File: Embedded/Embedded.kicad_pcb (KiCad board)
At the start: 2 copper layers, 77.5 x 106.5 mm, 95 parts, among them J1 GyroBreakout, J2 Conn_01x08, J3 Conn_01x08, J6 Conn_01x08, J7 Conn_01x08, SW1 BackboardSw, U1 ESP32-C6-WROOM-1, U2 BQ25895RTW, U3 FSUSB30MUX, U5 MP8715, U7 SN74AHCT125N, U8 SN74AHCT125N

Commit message: v2.1
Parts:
- added ?: , , F.Cu at (177.5, 95.6)
- added ?: , , F.Cu at (176.5, 96.7)
- added ?: , , F.Cu at (176.5, 98.2)
- moved LS1 41.9 mm to (175.0, 138.0), turned to -90 degrees
- moved ? 4.01 mm to (180.5, 95.5)
- moved ? 4.00 mm to (183.5, 95.5)
- moved ? 4.00 mm to (182.0, 95.5)
- moved ? 4.00 mm to (186.5, 95.5)
- moved ? 4.00 mm to (185.0, 95.5)
- moved ? 3.99 mm to (179.0, 95.5)
- moved ? 1.57 mm to (177.2, 111.2)
- moved ? 1.15 mm to (176.4, 99.6)
- moved ? 1.00 mm to (176.2, 110.1)
- moved ? 0.65 mm to (176.3, 108.6)
- moved ? 0.60 mm to (176.3, 107.1)
- moved ? 0.59 mm to (176.4, 101.1)
- moved ? 0.59 mm to (176.3, 105.6)
- moved ? 0.59 mm to (176.3, 102.6)
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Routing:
- net Net-(U1-MTMS/GPIO4/ADC1_CH4): track 0.00 -> 138.5 mm, vias 0 -> 6
- net Net-(U1-GPIO21): track 0.00 -> 118.6 mm, vias 0 -> 4
- net Net-(U1-MTDI/GPIO5/ADC1_CH5): track 60.0 -> 137.1 mm, vias 4 -> 6
- net GND: track 24.2 -> 9.09 mm, vias 50 -> 54
- net Net-(J6-Pin_6): track 28.9 -> 21.0 mm
- net Net-(J1-Pin_8): track 149.9 -> 152.6 mm
- net Net-(J1-Pin_7): track 144.5 -> 146.9 mm
- net +3.3V: track 329.1 -> 327.8 mm
- added copper zone on B.Cu, net GND
- added copper zone on F.Cu, net GND

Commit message: small changes, big dreams
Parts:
- added D1: 1N5819, Diode_THT:D_DO-41_SOD81_P10.16mm_Horizontal, B.Cu at (180.5, 75.4)
- added D2: 1N5819, Diode_THT:D_DO-41_SOD81_P10.16mm_Horizontal, B.Cu at (144.5, 45.0)
- added M1: Fan, Capacitor_SMD:C_1808_4520Metric_Pad1.72x2.30mm_HandSolder, F.Cu at (173.5, 75.5)
- added Q1: FQP27P06, Package_TO_SOT_THT:TO-220-3_Vertical, B.Cu at (173.9, 80.5)
- moved BT1 15.5 mm to (176.0, 92.5), turned to 0 degrees
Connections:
- J1 pad 3: unconnected-(J1-Pin_3-Pad3) -> Net-(J1-Pin_3)
- U1 pad 24: unconnected-(U1-U0RXD/GPIO17-Pad24) -> Net-(J1-Pin_3)
- U1 pad 25: unconnected-(U1-U0TXD/GPIO16-Pad25) -> Net-(Q1-G)
- U7 pad 11: Net-(J3-Pin_7) -> Net-(J3-Pin_4)
- U7 pad 3: Net-(J3-Pin_4) -> Net-(J3-Pin_7)
- U7 pad 6: Net-(J3-Pin_5) -> Net-(J3-Pin_6)
- U7 pad 8: Net-(J3-Pin_6) -> Net-(J3-Pin_5)
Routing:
- net Net-(Q1-G): track 0.00 -> 70.0 mm
- net Net-(J1-Pin_3): track 0.00 -> 30.9 mm, vias 0 -> 2
- net Net-(D1-A): track 0.00 -> 16.0 mm
- net +5V: track 199.9 -> 212.5 mm, vias 0 -> 1
- net Net-(J3-Pin_6): track 42.1 -> 33.1 mm
- net Net-(J3-Pin_5): track 30.5 -> 39.5 mm
- net Net-(J3-Pin_7): track 41.5 -> 32.5 mm, vias 1 -> 0
- net Net-(J3-Pin_4): track 24.8 -> 33.8 mm
- net Net-(BT1-+): track 221.2 -> 215.8 mm
- net Net-(J1-Pin_8): track 152.6 -> 155.7 mm
- net Net-(D2-K): track 19.2 -> 22.3 mm
- net Net-(J1-Pin_7): track 146.9 -> 149.6 mm
- net Net-(J2-Pin_3): track 17.4 -> 16.1 mm
- net +3.3V: track 327.8 -> 327.0 mm
- net GND: vias 54 -> 53

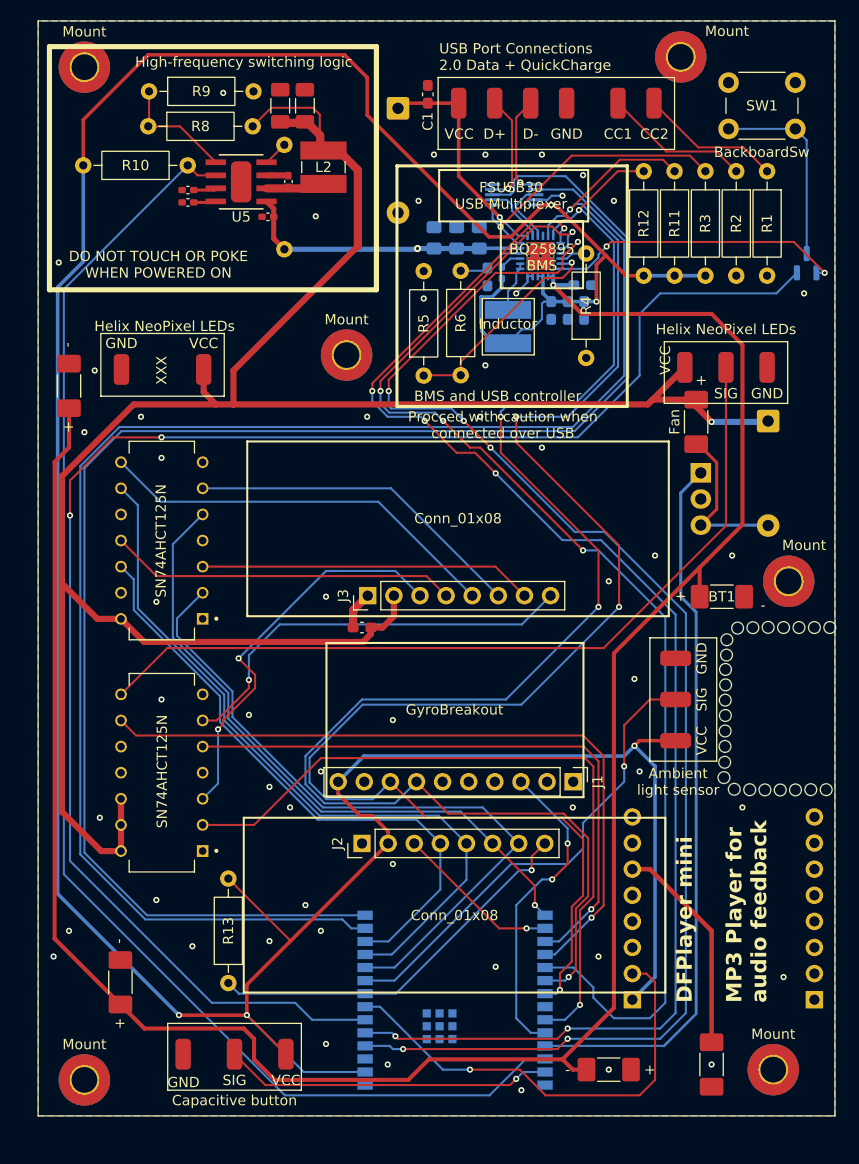
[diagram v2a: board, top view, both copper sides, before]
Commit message: Old model, new connectors
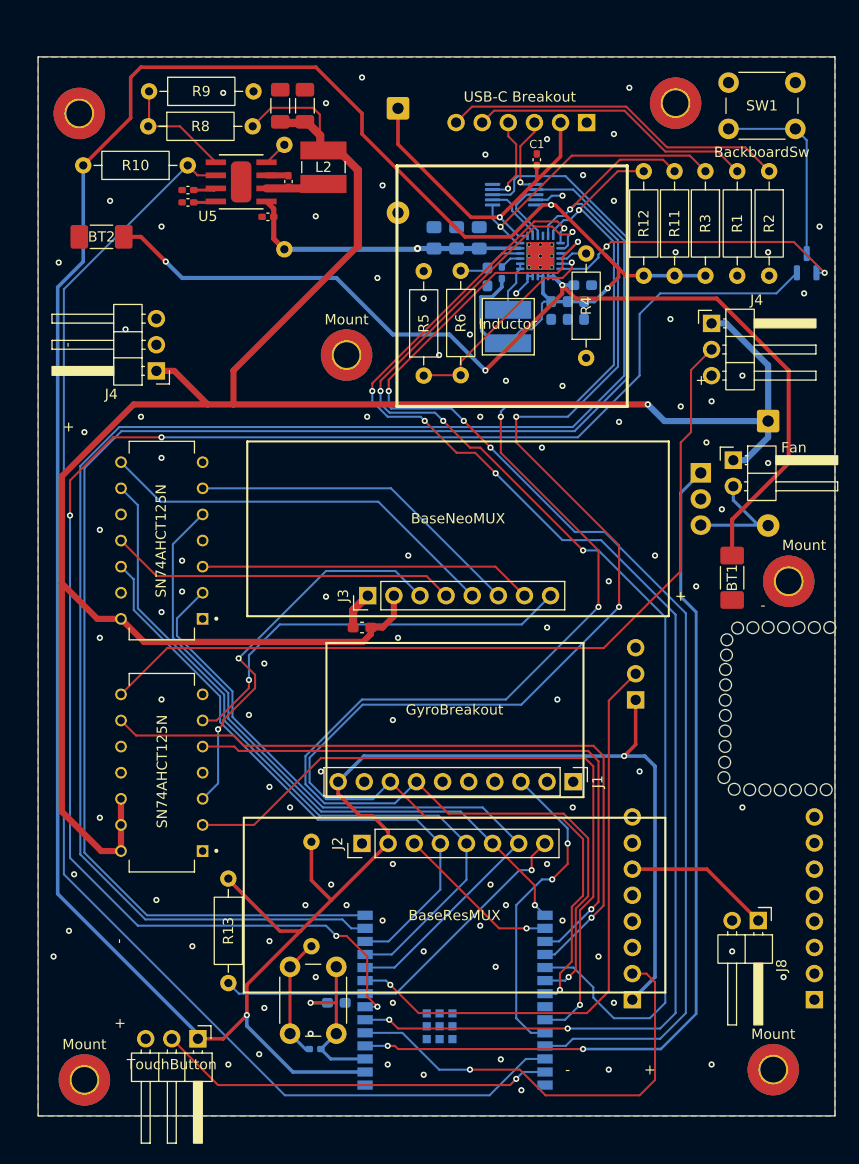
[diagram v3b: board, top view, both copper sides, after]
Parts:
- removed ALS1, H9, Neo3 (x2), Touch3: GND, Connector_Wire:SolderWirePad_1x01_SMD_1.5x3mm
- removed ALS2, Neo2, Touch2: SIG, Connector_Wire:SolderWirePad_1x01_SMD_1.5x3mm
- removed ALS3, H12, Neo1 (x2), Touch1: VCC, Connector_Wire:SolderWirePad_1x01_SMD_1.5x3mm
- removed the BT2 at (165.0, 138.5)
- removed the BT2 at (112.5, 72.0)
- removed the BT2 at (117.5, 130.0)
- removed H10: CC1, Connector_Wire:SolderWirePad_1x01_SMD_1.5x3mm
- removed H11: CC2, Connector_Wire:SolderWirePad_1x01_SMD_1.5x3mm
- removed H7: D-, Connector_Wire:SolderWirePad_1x01_SMD_1.5x3mm
- removed H8: D+, Connector_Wire:SolderWirePad_1x01_SMD_1.5x3mm
- removed LS1: Speaker, Capacitor_SMD:C_1808_4520Metric_Pad1.72x2.30mm_HandSolder
- removed M1: Fan, Capacitor_SMD:C_1808_4520Metric_Pad1.72x2.30mm_HandSolder
- added BT2: Battery_Cell, Capacitor_SMD:C_1808_4520Metric_Pad1.72x2.30mm_HandSolder, F.Cu at (115.7, 57.5)
- added C17: 100nF, Capacitor_SMD:C_0402_1005Metric_Pad0.74x0.62mm_HandSolder, B.Cu at (136.4, 136.5)
- added C18: 1uF, Capacitor_SMD:C_0603_1608Metric_Pad1.08x0.95mm_HandSolder, B.Cu at (138.5, 132.0)
- added J10: TouchButton, Connector_PinHeader_2.54mm:PinHeader_1x03_P2.54mm_Horizontal, F.Cu at (125.0, 135.5)
- added J11: USB-C Breakout, Connector_PinHeader_2.54mm:PinHeader_1x06_P2.54mm_Horizontal, B.Cu at (162.8, 46.4)
- added J4: HelixNeo, Connector_PinHeader_2.54mm:PinHeader_1x03_P2.54mm_Horizontal, F.Cu at (121.0, 70.5)
- added J4: HelixNeo, Connector_PinHeader_2.54mm:PinHeader_1x03_P2.54mm_Horizontal, F.Cu at (175.0, 65.9)
- added J5: Fan, Connector_PinHeader_2.54mm:PinHeader_1x02_P2.54mm_Horizontal, F.Cu at (177.1, 79.2)
- added J8: Speaker, Connector_PinHeader_2.54mm:PinHeader_1x02_P2.54mm_Horizontal, F.Cu at (179.5, 124.0)
- added J9: LightSensor, Connector_PinHeader_2.54mm:PinHeader_1x03_P2.54mm_Horizontal, B.Cu at (167.6, 102.5)
- added R14: 10k, Resistor_THT:R_Axial_DIN0207_L6.3mm_D2.5mm_P10.16mm_Horizontal, B.Cu at (136.1, 126.5)
- added SW2: BackboardSw, Button_Switch_THT:SW_PUSH_6mm_H5mm, F.Cu at (138.5, 128.5)
- C1: footprint Capacitor_SMD:C_0603_1608Metric_Pad1.08x0.95mm_HandSolder -> Capacitor_SMD:C_0402_1005Metric_Pad0.74x0.62mm_HandSolder
- C13: value 10nF -> 100nF
- J2: value Conn_01x08 -> BaseResMUX
- J3: value Conn_01x08 -> BaseNeoMUX
- R13: value 4.7k -> 10k
- moved C1 12.4 mm to (158.0, 50.0)
- moved Mount 4.53 mm to (113.5, 45.5)
- moved Mount 4.53 mm to (171.5, 44.5)
- moved R2 3.20 mm to (180.6, 51.1)
- moved R1 2.90 mm to (177.5, 51.1)
- moved BT1 2.09 mm to (177.0, 90.7), turned to -90 degrees
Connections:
- net Net-(BT1-+) renamed /Battery
- net Net-(D1-A) renamed /FanOut
- net Net-(D2-K) renamed /UsbVBUS
- net Net-(J1-Pin_3) renamed /GyroInt
- net Net-(J1-Pin_7) renamed /SDA
- net Net-(J1-Pin_8) renamed /SCL
- net Net-(J2-Pin_3) renamed /BaseResEN
- net Net-(J2-Pin_4) renamed /MuxS0
- net Net-(J2-Pin_5) renamed /MuxS1
- net Net-(J2-Pin_6) renamed /MuxS2
- net Net-(J2-Pin_7) renamed /MuxS3
- net Net-(J2-Pin_8) renamed /BaseResSIG
- net Net-(J3-Pin_4) renamed /BaseNeoS0
- net Net-(J3-Pin_5) renamed /BaseNeoS1
- net Net-(J3-Pin_6) renamed /BaseNeoS2
- net Net-(J3-Pin_7) renamed /BaseNeoS3
- net Net-(U1-GPIO12/USB_D-) renamed /EspD-
- net Net-(U1-GPIO13/USB_D+) renamed /EspD+
- net Net-(U1-GPIO15) renamed /BaseNeoEN
- net Net-(U1-GPIO19) renamed /BaseNeoSIG
- net Net-(U1-GPIO20) renamed /HelixNeoSIG
- net Net-(U1-GPIO21) renamed /BmsOTG
- net Net-(U1-GPIO3/ADC1_CH3) renamed /BuckPOK
- net Net-(U2-DSEL) renamed /UsbDSEL
- net Net-(U2-~{QON}) renamed /BackboardIcBtn
- D3 pad 2: Net-(U1-MTCK/GPIO6/ADC1_CH6) -> /BackboardBtn
- J6 pad 2: Net-(J6-Pin_2) -> /DFPlayer
- J6 pad 6: Net-(J6-Pin_6) -> /Spk+
- Q1 pad 1: Net-(Q1-G) -> /FanControl
- U1 pad 25: Net-(Q1-G) -> /BmsCE
- U1 pad 27: Net-(U1-GPIO2/ADC1_CH2) -> /TouchBtn
- U1 pad 3: unconnected-(U1-EN/CHIP_PU-Pad3) -> Net-(U1-EN/CHIP_PU)
- U1 pad 4: Net-(U1-MTMS/GPIO4/ADC1_CH4) -> /FanControl
- U1 pad 5: Net-(U1-MTDI/GPIO5/ADC1_CH5) -> /DFPlayer
- U1 pad 6: Net-(U1-MTCK/GPIO6/ADC1_CH6) -> /BmsInt
- U1 pad 7: Net-(J6-Pin_2) -> /BackboardBtn
- U1 pad 9: Net-(U1-GPIO1/ADC1_CH1/XTAL_32K_N) -> /ALS
- U2 pad 7: Net-(U1-MTDI/GPIO5/ADC1_CH5) -> /BmsInt
- U2 pad 9: Net-(U1-MTMS/GPIO4/ADC1_CH4) -> /BmsCE
- U3 pad 4: Net-(U3-D+) -> /UsbD+
- U3 pad 6: Net-(U3-D-) -> /UsbD-
- U8 pad 8: Net-(U8-3Y) -> /HelixNeo
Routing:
- net /BackboardBtn: track 0.00 -> 158.7 mm, vias 0 -> 4
- net Net-(U1-MTCK/GPIO6/ADC1_CH6): track 154.7 -> 0.00 mm, vias 2 -> 0
- net Net-(U1-MTMS/GPIO4/ADC1_CH4): track 138.2 -> 0.00 mm, vias 6 -> 0
- net Net-(U1-MTDI/GPIO5/ADC1_CH5): track 137.1 -> 0.00 mm, vias 6 -> 0
- net /BmsInt: track 0.00 -> 136.8 mm, vias 0 -> 6
- net /BmsCE: track 0.00 -> 120.4 mm, vias 0 -> 4
- net /Battery: track 215.8 -> 100.6 mm, vias 1 -> 3
- net /FanControl: track 0.00 -> 87.8 mm, vias 0 -> 2
- net /HelixNeo: track 0.00 -> 82.2 mm
- net Net-(U8-3Y): track 81.0 -> 0.00 mm
- net Net-(Q1-G): track 70.0 -> 0.00 mm
- net /ALS: track 0.00 -> 57.8 mm, vias 0 -> 1
- net Net-(U1-GPIO1/ADC1_CH1/XTAL_32K_N): track 46.2 -> 0.00 mm, vias 1 -> 0
- net Net-(J6-Pin_2): track 44.4 -> 0.00 mm, vias 1 -> 0
- net /DFPlayer: track 0.00 -> 43.4 mm, vias 0 -> 1
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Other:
- board size 77.5 x 106.5 mm -> 77.5 x 103 mm
- board text removed: "Ambient light sensor"
- board text removed: "BMS and USB controller"
- board text removed: "BQ25895 BMS"
- board text removed: "Capacitive button"
- board text removed: "DFPlayer mini MP3 Player for audio feedback"
- board text removed: "DO NOT TOUCH OR POKE WHEN POWERED ON"
- board text removed: "FSUSB30 USB Multiplexer"
- board text removed: "Helix NeoPixel LEDs"
- board text removed: "High-frequency switching logic"
- board text removed: "Procced with caution when connected over USB"
- board text removed: "USB Port Connections 2.0 Data + QuickCharge"
- board text removed: "XXX"

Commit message: v4
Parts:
- added ?: , , B.Cu at (154.2, 86.2)
- added ?: , , F.Cu at (162.8, 78.2)
- added BT3: Battery_Cell, Connector_JST:JST_PH_B2B-PH-K_1x02_P2.00mm_Vertical, F.Cu at (173.5, 110.8)
- added BT4: Battery_Cell, Connector_JST:JST_PH_B2B-PH-K_1x02_P2.00mm_Vertical, F.Cu at (173.5, 138.9)
- added F1: Polyfuse, Fuse:Fuse_1206_3216Metric_Pad1.42x1.75mm_HandSolder, B.Cu at (130.5, 64.5)
- added F2: Polyfuse, Fuse:Fuse_1206_3216Metric_Pad1.42x1.75mm_HandSolder, F.Cu at (118.5, 122.8)
- added F3: Polyfuse, Fuse:Fuse_1206_3216Metric_Pad1.42x1.75mm_HandSolder, F.Cu at (174.8, 116.8)
- added F4: Polyfuse, Fuse:Fuse_1206_3216Metric_Pad1.42x1.75mm_HandSolder, B.Cu at (173.5, 130.2)
- added HelixNeoSig-Cont: PinHeader_1x01_P2.54mm_Horizontal, Connector_PinHeader_2.54mm:PinHeader_1x01_P2.54mm_Horizontal, F.Cu at (121.8, 71.2)
- added Q2: FS8205A, Package_SO:MSOP-8_3x3mm_P0.65mm, B.Cu at (126.0, 61.5)
- added Q3: AO3401A, Package_TO_SOT_SMD:TSOT-23_HandSoldering, B.Cu at (118.5, 61.2)
- added Q4: FS8205A, Package_SO:MSOP-8_3x3mm_P0.65mm, F.Cu at (119.5, 129.5)
- added Q5: AO3401A, Package_TO_SOT_SMD:TSOT-23_HandSoldering, B.Cu at (112.2, 126.5)
- added Q6: FS8205A, Package_SO:MSOP-8_3x3mm_P0.65mm, B.Cu at (174.8, 119.8)
- added Q7: AO3401A, Package_TO_SOT_SMD:TSOT-23_HandSoldering, B.Cu at (178.2, 114.2)
- added Q8: FS8205A, Package_SO:MSOP-8_3x3mm_P0.65mm, B.Cu at (181.3, 132.4)
- added Q9: AO3401A, Package_TO_SOT_SMD:TSOT-23_HandSoldering, B.Cu at (167.8, 139.5)
- added R15: 100, Resistor_THT:R_Axial_DIN0207_L6.3mm_D2.5mm_P10.16mm_Horizontal, F.Cu at (127.3, 58.2)
- added R16: 100, Resistor_THT:R_Axial_DIN0207_L6.3mm_D2.5mm_P10.16mm_Horizontal, F.Cu at (110.8, 53.8)
- added R17: 100, Resistor_THT:R_Axial_DIN0207_L6.3mm_D2.5mm_P10.16mm_Horizontal, B.Cu at (119.5, 126.5)
- added R18: 100, Resistor_THT:R_Axial_DIN0207_L6.3mm_D2.5mm_P10.16mm_Horizontal, B.Cu at (123.5, 121.8)
- added R19: 100, Resistor_THT:R_Axial_DIN0207_L6.3mm_D2.5mm_P10.16mm_Horizontal, F.Cu at (179.5, 127.1)
- added R20: 100, Resistor_THT:R_Axial_DIN0207_L6.3mm_D2.5mm_P10.16mm_Horizontal, F.Cu at (182.5, 116.9)
- added R21: 100, Resistor_THT:R_Axial_DIN0207_L6.3mm_D2.5mm_P10.16mm_Horizontal, F.Cu at (173.5, 124.7)
- added R22: 100, Resistor_THT:R_Axial_DIN0207_L6.3mm_D2.5mm_P10.16mm_Horizontal, F.Cu at (176.5, 124.7)
- added U10: DW01A, Package_TO_SOT_SMD:SOT-23-6, B.Cu at (177.2, 131.2)
- added U4: DW01A, Package_TO_SOT_SMD:SOT-23-6, B.Cu at (122.1, 57.0)
- added U6: DW01A, Package_TO_SOT_SMD:SOT-23-6, B.Cu at (119.8, 131.5)
- added U9: DW01A, Package_TO_SOT_SMD:SOT-23-6, B.Cu at (180.5, 121.2)
- BT1, BT2: footprint Capacitor_SMD:C_1808_4520Metric_Pad1.72x2.30mm_HandSolder -> Connector_JST:JST_PH_B2B-PH-K_1x02_P2.00mm_Vertical
- C1, SW2: moved to B.Cu
- C18: moved to F.Cu
- J5: value Fan -> FanConnector
- Q1: footprint Package_TO_SOT_THT:TO-220-3_Vertical -> Package_TO_SOT_THT:TO-220-3_Horizontal_TabDown
- moved BT2 76.5 mm to (113.0, 134.0), turned to 90 degrees
- moved BT1 70.9 mm to (113.8, 58.5)
- moved J8 21.2 mm to (173.5, 103.7), turned to 0 degrees
- moved D2 7.52 mm to (146.5, 52.2), turned to 90 degrees
- moved SW2 7.00 mm to (138.5, 135.5), turned to 90 degrees
- moved C18 6.50 mm to (136.0, 138.0), turned to 0 degrees
- moved J4 3.00 mm to (118.0, 70.5)
- moved J9 1.75 mm to (168.0, 100.8)
- moved R6 1.56 mm to (149.0, 60.8)
- moved R5 1.00 mm to (146.0, 71.0)
- moved C9 1.00 mm to (152.3, 61.0), turned to 0 degrees
- moved C1 0.71 mm to (158.5, 49.5), turned to 180 degrees
- moved R14 0.59 mm to (136.5, 126.1)
- moved C2 0.41 mm to (152.0, 57.5)
- moved C3 0.22 mm to (150.0, 57.5)
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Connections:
- BT1 pad 1: /Battery -> Net-(BT1-+)
- BT1 pad 2: GND -> Net-(BT1--)
- BT2 pad 1: /Battery -> Net-(BT2-+)
- BT2 pad 2: GND -> Net-(BT2--)
- C8 pad 1: /Battery -> GND
- C8 pad 2: GND -> BATT
- J4 pad 2: (no net) -> HelixNeoSigCont
- U2 pad 13: /Battery -> BATT
- U2 pad 14: /Battery -> BATT
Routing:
- net BATT: track 0.00 -> 196.8 mm, vias 0 -> 7
- net /Battery: track 100.6 -> 0.00 mm, vias 3 -> 0
- net Net-(BT4--): track 0.00 -> 26.8 mm
- net Net-(BT1--): track 0.00 -> 23.2 mm, vias 0 -> 1
- net Net-(BT2--): track 0.00 -> 17.8 mm, vias 0 -> 1
- net Net-(BT3--): track 0.00 -> 16.6 mm
- net Net-(Q3-D): track 0.00 -> 15.0 mm
- net Net-(Q5-D): track 0.00 -> 13.7 mm
- net Net-(Q9-D): track 0.00 -> 12.6 mm
- net Net-(Q2-G2): track 0.00 -> 12.3 mm
- net +5V: track 228.2 -> 217.8 mm, vias 1 -> 3
- net Net-(U9-VCC): track 0.00 -> 9.61 mm, vias 0 -> 1
- net Net-(Q6-G1): track 0.00 -> 9.60 mm
- net Net-(Q6-G2): track 0.00 -> 8.14 mm
- net Net-(U9-CS): track 0.00 -> 7.92 mm
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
